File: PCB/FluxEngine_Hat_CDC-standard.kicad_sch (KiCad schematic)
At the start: 7 parts, among them J1 CY8CKIT-059, J2 Screw_Terminal_01x04, P1 FDC_BUS_IBMPC, P2 FDC_BUS_CDC_9406_STD, U1 74HC00

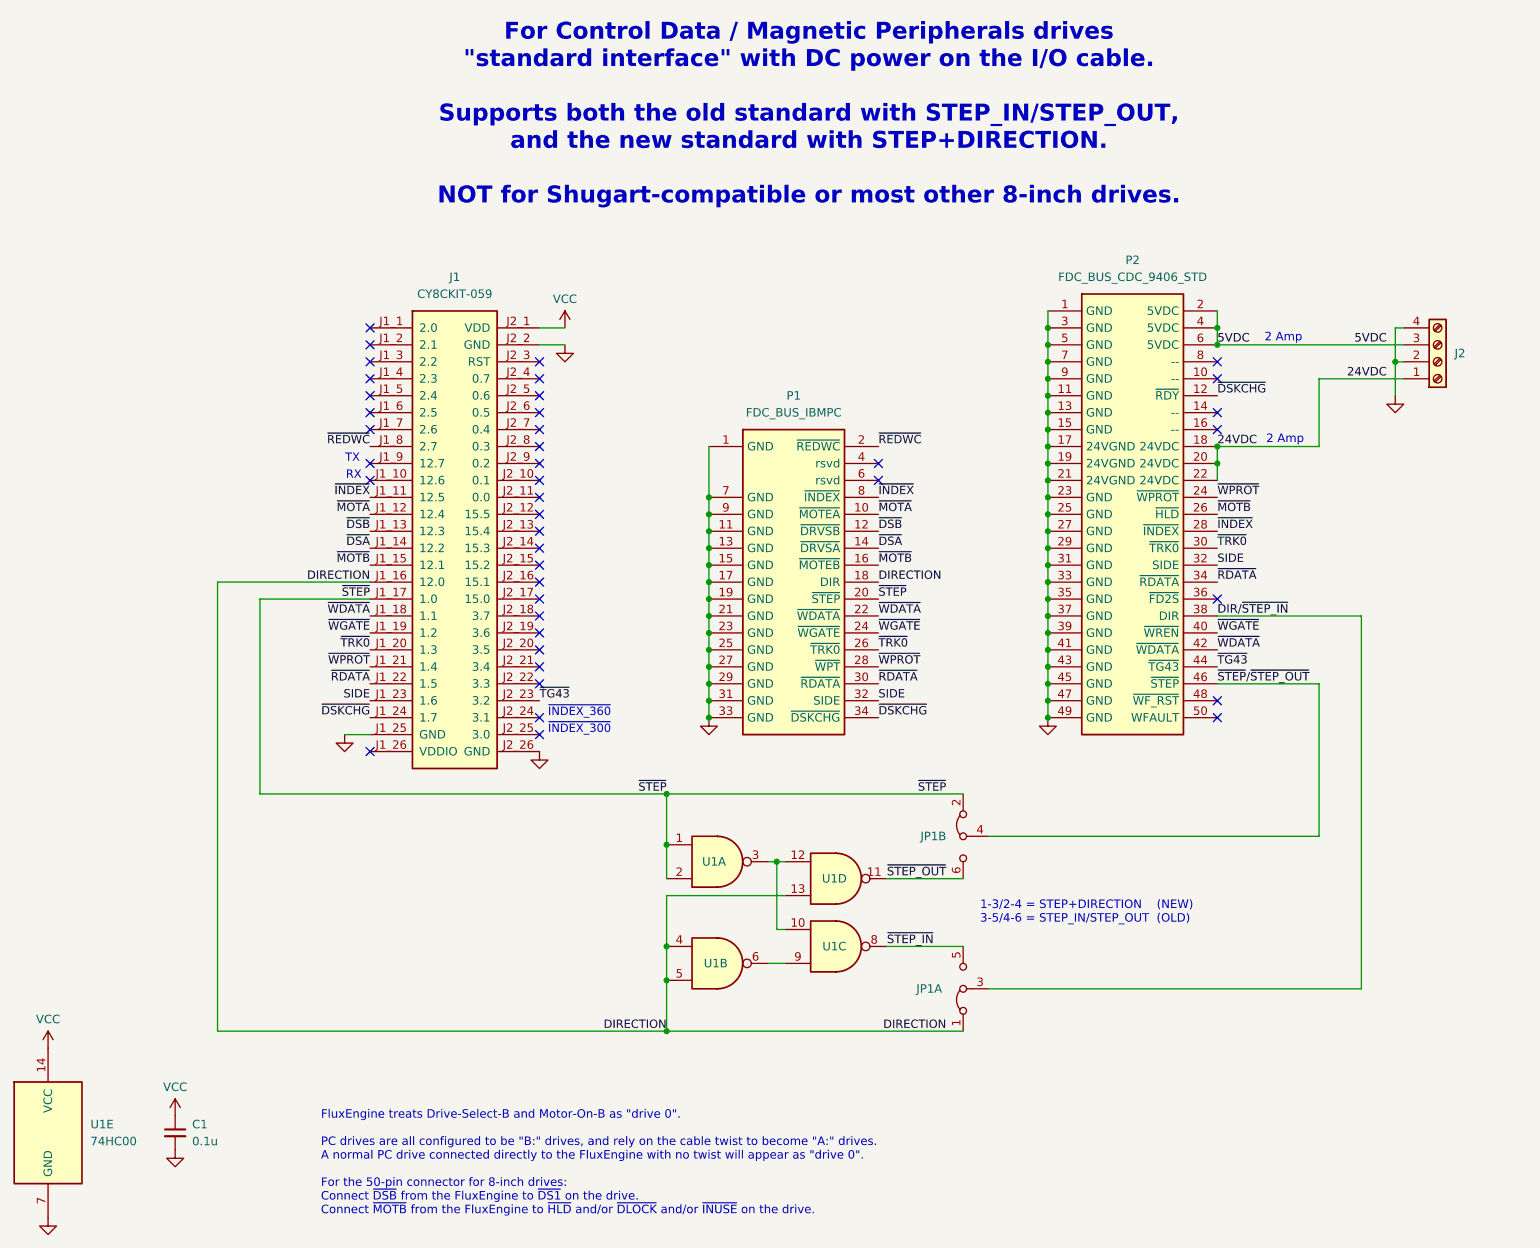
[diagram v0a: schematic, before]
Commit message: fix CDC-standard backwards step_in/step_out decoding
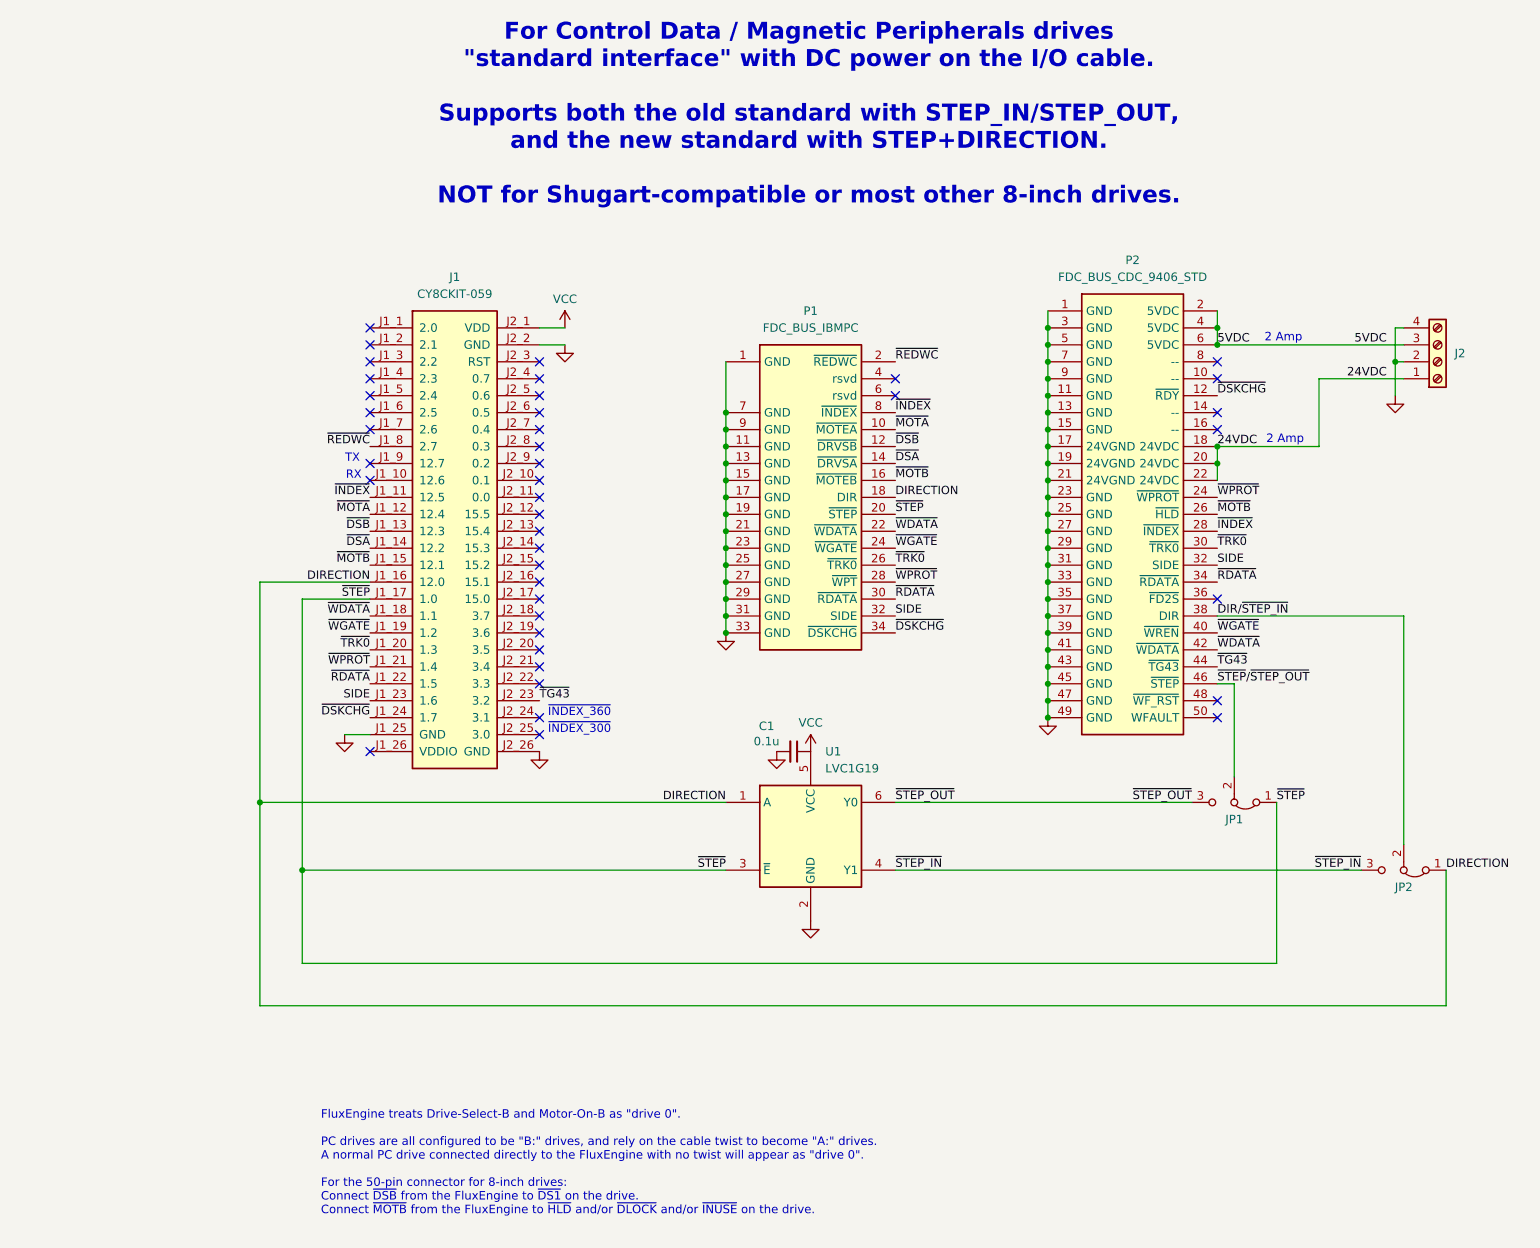
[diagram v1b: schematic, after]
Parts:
- removed JP1: Jumper_3_Bridged12_x_2, 000_LOCAL:PinHeader_2x03_P2.54mm_Vertical, symbol 000_LOCAL:Jumper_3_Bridged12_x_2
- removed U1: 74HC00, 000_LOCAL:TSSOP-14_4.4x5mm_P0.65mm, symbol 000_LOCAL:74HC00
- added JP1, JP2: Jumper_3_Bridged12, 000_LOCAL:PinHeader_1x03_P2.54mm_Vertical, symbol 000_LOCAL:Jumper_3_Bridged12
- added U1: LVC1G19, 000_LOCAL:SOT-363_SC-70-6, symbol 000_LOCAL:74LVC1G19
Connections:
- net DIRECTION: now also JP2.1 (A), U1.1 (A)
- net DIR/~{STEP_IN}: now also JP2.2 (C)
- net GND: now also U1.2 (GND)
- net VCC: now also U1.5 (VCC)
- net ~{STEP_IN}: now also JP2.3 (B), U1.4 (Y1)
- net ~{STEP_OUT}: now also JP1.3 (B), U1.6 (Y0)
- net ~{STEP}: now also JP1.1 (A), U1.3 (~{E})
- net ~{STEP}/~{STEP_OUT}: now also JP1.2 (C)
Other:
- note removed: "1-3/2-4 = STEP+DIRECTION (NEW) 3-5/4-6 = STEP_IN/STEP_OUT (OLD)"
- moved on the sheet: C1, P1

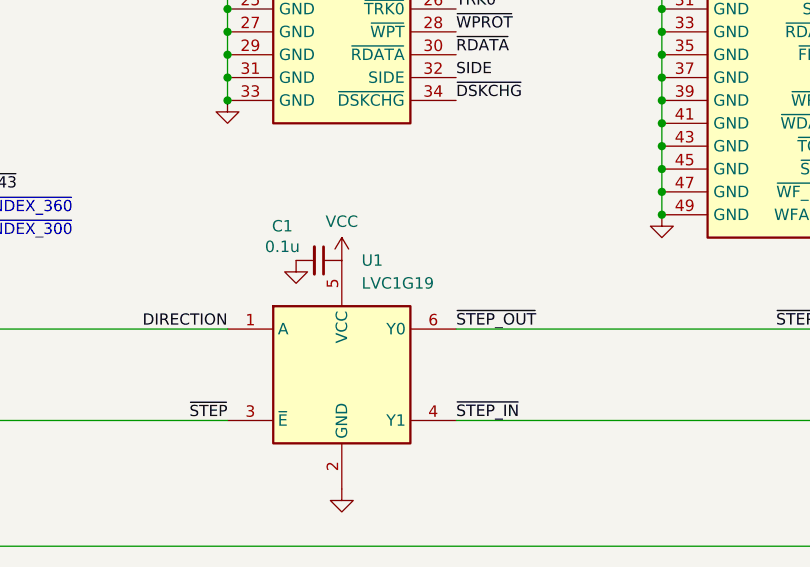
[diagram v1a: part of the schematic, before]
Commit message: rotate 1G19 for easier hand soldering
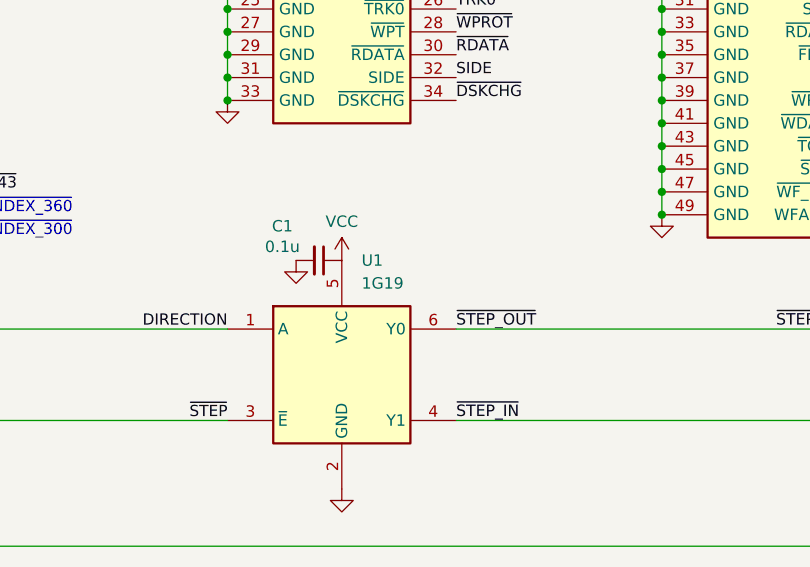
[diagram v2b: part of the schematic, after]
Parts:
- U1: value LVC1G19 -> 1G19
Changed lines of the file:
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@@
 			)
 		)
-		(property "Value" "LVC1G19"
+		(property "Value" "1G19"
 			(at 148.2441 129.54 0)
 			(effects

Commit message: staggered rows offset & direction
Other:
- title: FluxEngine_Hat for PC and CDC-standard -> FluxEngine_Hat_CDC-standard
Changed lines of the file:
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@@
 	(paper "User" 298.45 217.322)
 	(title_block
-		(title "FluxEngine_Hat for PC and CDC-standard")
-		(date "2024-04-30")
+		(title "FluxEngine_Hat_CDC-standard")
+		(date "2024-08-08")
 		(rev "004")
 		(company "Brian K. White - b.kenyon.w@gmail.com")
